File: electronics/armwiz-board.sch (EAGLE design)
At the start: 99 parts, among them J1 MICRO-SDCARD-CONNECTOR-330006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, J15 Cortex Debug, J16 ST-Link v2, J2 CORTEX_DEBUGSMD, U1 STM32F10XRXT6, U4 MIC5219-3.3V, X1 FH12-12S-1S, Y3 32.768kHz

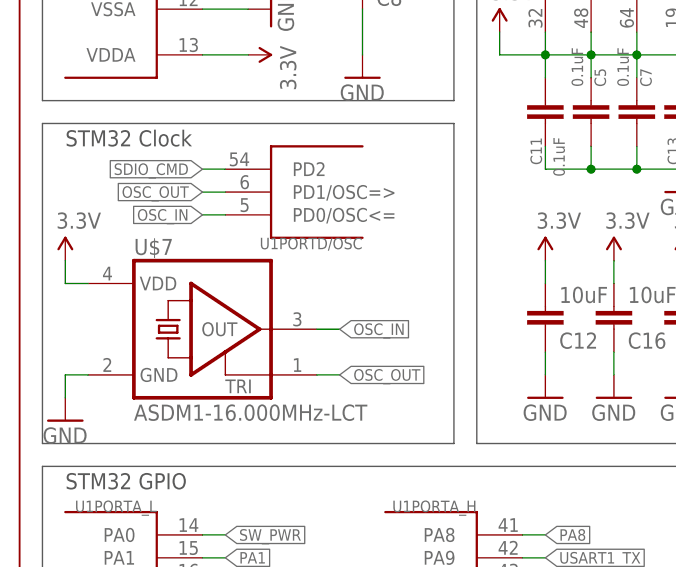
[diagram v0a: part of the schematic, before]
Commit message: Fixed MEMS oscillator issue. Closes #3.
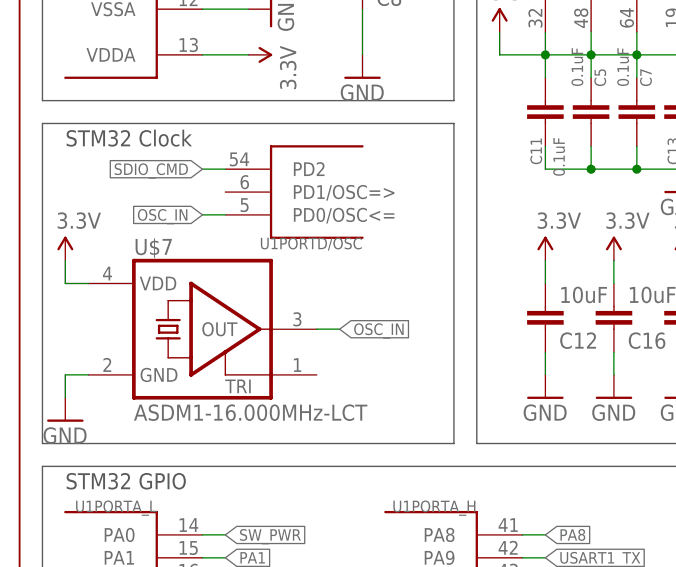
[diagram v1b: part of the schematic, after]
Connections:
- removed net OSC_OUT: U$7.TRI, U1PORTD/OSC.PD1/OSC=>
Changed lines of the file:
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@@
-</segment>
-</net>
-<net name="OSC_OUT" class="0">
-<segment>
-<pinref part="U1" gate="PORTD/OSC" pin="PD1/OSC=&gt;"/>
-<wire x1="30.48" y1="134.62" x2="27.94" y2="134.62" width="0.1524" layer="91"/>
-<label x="27.94" y="134.62" size="1.27" layer="95" rot="R180" xref="yes"/>
-</segment>
-<segment>
-<pinref part="U$7" gate="G$1" pin="TRI"/>
-<wire x1="40.64" y1="114.3" x2="43.18" y2="114.3" width="0.1524" layer="91"/>
-<label x="43.18" y="114.3" size="1.27" layer="95" xref="yes"/>
 </segment>
 </net>

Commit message: Board passes ERC and DRC.
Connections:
- removed net N$17: J2.GNDDTCT
- net GND: now also J2.GNDDTCT
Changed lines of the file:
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@@
 </variantdefs>
 <classes>
-<class number="0" name="default" width="0.075" drill="0.2">
+<class number="0" name="Digital signal" width="0.075" drill="0.2">
 <clearance class="0" value="0.075"/>
 </class>
-<class number="1" name="power" width="0.075" drill="0.2">
+<class number="1" name="3.3V power" width="0.075" drill="0.2">
 <clearance class="1" value="0.075"/>
+</class>
+<class number="2" name="RTC battery" width="0.075" drill="0.2">
+<clearance class="2" value="0.075"/>
+</class>
+<class number="3" name="5V power" width="0.075" drill="0.2">
+<clearance class="3" value="0.075"/>
+</class>
+<class number="4" name="Analog signal" width="0.075" drill="0.2">
+<clearance class="4" value="0.075"/>
+</class>
+<class number="5" name="Ground" width="0.075" drill="0.2">
+<clearance class="5" value="0.075"/>
 </class>
 </classes>
@@
 <wire x1="200.66" y1="152.4" x2="198.12" y2="152.4" width="0.1524" layer="91"/>
 <pinref part="J2" gate="G$1" pin="GND@3"/>
-<wire x1="198.12" y1="152.4" x2="198.12" y2="144.78" width="0.1524" layer="91"/>
+<wire x1="198.12" y1="152.4" x2="198.12" y2="147.32" width="0.1524" layer="91"/>
+<wire x1="198.12" y1="147.32" x2="198.12" y2="144.78" width="0.1524" layer="91"/>
 <wire x1="200.66" y1="154.94" x2="198.12" y2="154.94" width="0.1524" layer="91"/>
 <wire x1="198.12" y1="154.94" x2="198.12" y2="152.4" width="0.1524" layer="91"/>
 <junction x="198.12" y="152.4"/>
+<pinref part="J2" gate="G$1" pin="GNDDTCT"/>
+<wire x1="200.66" y1="147.32" x2="198.12" y2="147.32" width="0.1524" layer="91"/>
+<junction x="198.12" y="147.32"/>
 </segment>
 <segment>
@@
 </segment>
 </net>
-<net name="RTC_BAT" class="0">
+<net name="RTC_BAT" class="2">
 <segment>
 <pinref part="U1" gate="AN_POWER" pin="VBAT"/>
@@
 <pinref part="J2" gate="G$1" pin="SWDIO/TMS"/>
 <wire x1="238.76" y1="157.48" x2="233.68" y2="157.48" width="0.1524" layer="91"/>
-</segment>
-</net>
-<net name="N$17" class="0">
-<segment>
-<pinref part="J2" gate="G$1" pin="GNDDTCT"/>
-<wire x1="200.66" y1="147.32" x2="195.58" y2="147.32" width="0.1524" layer="91"/>
-<label x="195.58" y="147.32" size="1.27" layer="95" rot="R180" xref="yes"/>
 </segment>
 </net>
@@
 </sheet>
 </sheets>
+<errors>
+</errors>
 </schematic>
 </drawing>

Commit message: Changed to a metric layout. Moved to a 7x2 2.0mm module connector.
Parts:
- removed J$1: SMA_EDGE, SparkFun-Connectors:SMA_EDGE
- removed J10, J11, J12, J13, J19, J20, J21, J22, J23, J24, J26, J27, J3, J33, J4, J5, J6, J7, J8: (no value), SparkFun-Connectors:M01PTH
- removed J14: (no value), PaxInstruments-Connectors:M03X2PAX
- removed J15: Cortex Debug, SparkFun-Connectors:CORTEX_DEBUGSMD
- removed J16: ST-Link v2, SparkFun-Connectors:M10X2
- removed J17, J18: (no value), SparkFun-Connectors:M01NOSILK-KIT
- removed R23: 100R, resistor:R-US_R0402
- removed R24: 10K, resistor:R-US_R0402
- added C19, C20: 8pF, resistor:C-EUC0402K
- added C21: 10uF, resistor:C-EUC0402K
- added U$4, U$8, U$9: PAX_MODULE, PaxInstruments-Connectors:PAX_MODULE
- added Y1: 32.768kHz, SparkFun-FreqCtrl:CRYSTAL3.2X1.5MM
- U$7: value ASDM1-16.000MHz-LCT -> PAX_MODULE; device crystal:ASE -> PaxInstruments-Connectors:PAX_MODULE
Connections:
- net BOOT1 renamed (BOOT1)
- net MISO3 renamed PB4
- net MOSI3 renamed LCD_MOSI_(SPI3_MOSI)
- net RTC1 renamed RTC_OSC_IN
- net RTC2 renamed RTC_OSC_OUT
- net SCK3 renamed LCD_SCK_(SPI3_SCK)
- net SW_PWR renamed SW_PWR_(SYS_WKUP)
- net USB+ renamed USB_DP
- net USB- renamed USB_DM
- removed net AD_GND: J15.GND@3, J15.GND@5, J15.GNDDTCT, J16.10, J16.12, J16.14, J16.16, J16.18, J16.20, J16.4, J16.6, J16.8
- removed net AD_NRST: J15.NRESET, J16.15
- removed net AD_SWDCLK: J15.SWDCLK/TCK, J16.9
- removed net AD_SWDIO: J15.SWDIO/TMS, J16.7
- removed net AD_SWO: J15.SWO/TDO, J16.13
- removed net AD_TDI: J15.NC/TDI, J16.5
- removed net AD_VCC: J15.VCC, J16.1
- removed net LCD_A0: U1PORTB_H.PB9, X1-8.1
- removed net LCD_BL: R19.2, U1PORTB_L.PB6
- removed net LCD_CS: U1PORTB_L.PB7, X1-10.1
- removed net LCD_RST: U1PORTB_H.PB8, X1-9.1
- removed net MISO1: J10.1, U1PORTA_L.PA6
- removed net MOSI1: J13.1, U1PORTA_L.PA7
- removed net N$12: J2.SWO/TDO, R23.2
- removed net N$14: J$1.GND@1, J$1.GND@3, J26.1
- removed net N$15: J$1.GND@0, J$1.GND@2, J23.1
- removed net N$20: J$1.SIGNAL, J27.1
- removed net PA2: J3.1, U1PORTA_L.PA2
- removed net PA3: J12.1, U1PORTA_L.PA3
- removed net PA4: J5.1, U1PORTA_L.PA4
- removed net PB10: J24.1, U1PORTB_H.PB10
- removed net PC0: J20.1, U1PORTC_L.PC0
- removed net PC1: J22.1, U1PORTC_L.PC1
- removed net PC13: J21.1, U1PORTC_H.PC13
- removed net SCLK1: J4.1, U1PORTA_L.PA5
- removed net SWDCLK: J14.2, R18.1, R2.1, U1PORTA_H.PA14
- removed net SWO: J14.6, R23.1, R24.1, U1PORTA_H.PA15
- removed net VBAT2: R25.2, R26.1, U1PORTC_L.PC5
- new net 12C1_SDA: U1PORTB_L.PB7
- new net CAN_RX: U$4.CAN_RX, U$7.CAN_RX, U$8.CAN_RX, U$9.CAN_RX, U1PORTB_H.PB8
- new net CAN_TX: U$4.CAN_TX, U$7.CAN_TX, U$8.CAN_TX, U$9.CAN_TX, U1PORTB_H.PB9
- new net GPIO_(SPI1_NSS): U$8.GPIO0_(INT/A/D), U1PORTA_L.PA4
- new net GPIO_(SPI2_NSS): U$4.GPIO0_(INT/A/D), U1PORTB_H.PB12
- new net I2C1_SCL: U$4.I2C_SCL, U$7.I2C_SCL, U1PORTB_L.PB6
- new net I2C1_SDA: U$4.I2C_SDA, U$7.I2C_SDA
- new net I2C2_SCL: U$8.I2C_SCL, U$9.I2C_SCL, U1PORTB_H.PB10
- new net I2C2_SDA: U$8.I2C_SDA, U$9.I2C_SDA, U1PORTB_H.PB11
- new net LCD_A0_(GPIO): U1PORTC_L.PC1, X1-8.1
- new net LCD_BL_(GPIO): R19.2, U1PORTC_L.PC0
- new net LCD_CS_(SPI3_NSS): U1PORTA_H.PA15, X1-10.1
- new net LCD_RST_(GPIO): U1PORTC_H.PC13, X1-9.1
- new net LED2: LED2.A
- new net N$51: U$8.GPIO1_(INT/A/D)
- new net N$52: U$8.GPIO2_(INT/A/D)
- new net N$57: U$4.GPIO1_(INT/A/D)
- new net N$58: U$4.GPIO2_(INT/A/D)
- new net N$68: U$7.GPIO0_(INT/A/D)
- new net N$69: U$7.GPIO1_(INT/A/D)
- new net N$70: U$7.GPIO2_(INT/A/D)
- new net N$74: U$9.GPIO0_(INT/A/D)
- new net N$75: U$9.GPIO1_(INT/A/D)
- new net N$76: U$9.GPIO2_(INT/A/D)
- new net OSC_OUT: C19.1, U1PORTD/OSC.PD1/OSC=>, Y1.1
- new net PC5: U1PORTC_L.PC5
- new net PC6: U1PORTC_L.PC6
- new net PC7: U1PORTC_L.PC7
- new net SPI1_MISO: U$8.SPI_MISO, U$9.SPI_MISO, U1PORTA_L.PA6
- new net SPI1_MOSI: U$8.SPI_MOSI, U$9.SPI_MOSI, U1PORTA_L.PA7
- new net SPI1_SCK: U$8.SPI_SCK, U$9.SPI_SCK, U1PORTA_L.PA5
- new net SPI2_MISO: U$4.SPI_MISO, U$7.SPI_MISO, U1PORTB_H.PB14
- new net SPI2_MOSI: U$4.SPI_MOSI, U$7.SPI_MOSI, U1PORTB_H.PB15
- new net SPI2_SCK: U$4.SPI_SCK, U$7.SPI_SCK, U1PORTB_H.PB13
- new net SWCLK: R18.1, R2.1, U1PORTA_H.PA14
- new net USART2_RX: U$4.USART_RX, U$7.USART_RX, U$8.USART_RX, U$9.USART_RX, U1PORTA_L.PA3
- new net USART2_TX: U$4.USART_TX, U$7.USART_TX, U$8.USART_TX, U$9.USART_TX, U1PORTA_L.PA2
- new net VBAT_1/2: R25.2, R26.1
- net 3.3V: now also C21.2, U$4.3V3, U$7.3V3, U$8.3V3, U$9.3V3; no longer J14.1, J18.1, R24.2, U$7.VDD
- net BOOT0: no longer J17.1
- net GND: now also C19.2, C20.2, C21.1, U$4.GND, U$8.GND, U$9.GND; no longer J14.3
- net NRST: no longer J14.5
- net OSC_IN: now also C20.1, Y1.2; no longer U$7.OUT
- net PA1: no longer J19.1
- net PA8: no longer LED2.A
- net PB0: no longer J6.1
- net PB1: no longer J11.1
- net PC2: no longer J33.1
- net PC3: no longer J7.1
- net PC4: no longer J8.1
- net SD_DETECT: no longer U1PORTB_H.PB14
- net SWDIO: no longer J14.4
- net SW_A: no longer U1PORTB_H.PB15
- net SW_B: no longer U1PORTC_L.PC6
- net SW_C: no longer U1PORTC_L.PC7
- net SW_D: no longer U1PORTB_H.PB12
- net SW_E: no longer U1PORTB_H.PB13
- net VBUS: no longer U1PORTB_H.PB11
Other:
- note added: "Breakout Headers"
- note added: "Orphin Nets"
- note removed: "Board edgs SMA connector"
- note removed: "Breakout Header"
- note removed: "Cortex Debug Adapter"
- note removed: "Testing Suff"
- moved on the sheet: BAT1, C14, C6, C9, J1, R13, R14, R17, R5, R6, R7, Y3

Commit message: Updated board with new Pax Instruments library parts.
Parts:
- removed U$4, U$7, U$8, U$9: PAX_MODULE, PaxInstruments-Connectors:PAX_MODULE
- removed X1: FH12-12S-1S, PaxInstrument-T400:FH12-12S-1S
- added MODULE1, MODULE2, MODULE3, MODULE4: PI-module-female, PaxInstruments-Connectors:PAX_MODULE_EDGE_FEMALE_HOST
- added X2: M12_BOTTOM_CONTACTS_FPC_1MM, PaxInstruments-Connectors:M12_BOTTOM_CONTACTS_FPC_1MM
- C1: device resistor:C-EUC0402K -> PaxInstruments-Capacitors:C0402_4.7UF
- C10, C11, C13, C14, C15, C18, C2, C27, C3, C5, C7, C8: device resistor:C-EUC0402K -> PaxInstruments-Capacitors:C0402_100NF
- C12, C16, C17, C21, C26: device resistor:C-EUC0402K -> PaxInstruments-Capacitors:C0402_10UF
- C19, C20, C6, C9: device resistor:C-EUC0402K -> PaxInstruments-Capacitors:C0402_8PF
- C35, C36: device resistor:C-EUC0402K -> PaxInstruments-Capacitors:C0402_1UF
- C4: device resistor:C-EUC0402K -> PaxInstruments-Capacitors:C0402_470PF
- J1: value MICRO-SDCARD-CONNECTOR-3300060P1 -> MICROSD; device PaxInstrument-T400:MICRO-SDCARD-CONNECTOR-3300060P1 -> PaxInstruments-Connectors:MICROSD; MF SUNTECH -> (none)
- R1, R11, R12, R15, R16, R8: value 10k -> 10K; device resistor:R-US_R0402 -> PaxInstruments-Resistors:R0402_10K; POPULATE DNP -> (none)
- R10, R9: device resistor:R-US_R0402 -> PaxInstruments-Resistors:R0402_22R
- R13, R14, R17, R2, R21, R25, R26, R4, R5, R6, R7: device resistor:R-US_R0402 -> PaxInstruments-Resistors:R0402_10K
- R18, R20: device resistor:R-US_R0402 -> PaxInstruments-Resistors:R0402_100R
- R19: device resistor:R-US_R0402 -> PaxInstruments-Resistors:R0402_3.3R
- R22, R3: device resistor:R-US_R0402 -> PaxInstruments-Resistors:R0402_360R
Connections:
- removed net 12C1_SDA: U1PORTB_L.PB7
- removed net N$52: U$8.GPIO2_(INT/A/D)
- removed net N$58: U$4.GPIO2_(INT/A/D)
- removed net N$70: U$7.GPIO2_(INT/A/D)
- removed net N$76: U$9.GPIO2_(INT/A/D)
- removed net PB4: U1PORTB_L.PB4
- new net PC0: U1PORTC_L.PC0
- net 3.3V: now also C11.1, C12.1, C13.1, C16.1, C17.1, C21.1, C26.2, C27.2, C8.1, MODULE1.3V3, MODULE2.3V3, MODULE3.3V3, MODULE4.3V3, R13.2, R14.2, R17.2, R5.2, R6.2, R7.2, X2.12, X2.5; no longer C11.2, C12.2, C13.2, C16.2, C17.2, C21.2, C26.1, C27.1, C8.2, R13.1, R14.1, R17.1, R5.1, R6.1, R7.1, U$4.3V3, U$7.3V3, U$8.3V3, U$9.3V3, X1-12.1, X1-5.1
- net CAN_RX: now also MODULE1.CAN_RX, MODULE2.CAN_RX, MODULE3.CAN_RX, MODULE4.CAN_RX; no longer U$4.CAN_RX, U$7.CAN_RX, U$8.CAN_RX, U$9.CAN_RX
- net CAN_TX: now also MODULE1.CAN_TX, MODULE2.CAN_TX, MODULE3.CAN_TX, MODULE4.CAN_TX; no longer U$4.CAN_TX, U$7.CAN_TX, U$8.CAN_TX, U$9.CAN_TX
- net GND: now also C1.1, C11.2, C12.2, C13.2, C16.2, C17.2, C2.1, C21.2, C26.1, C27.1, C8.2, J1.GND1, J1.GND2, J1.GND3, J1.GND4, MODULE1.GND, MODULE1.KEY, MODULE2.GND, MODULE2.KEY, MODULE3.GND, MODULE3.KEY, MODULE4.GND, MODULE4.KEY, R1.1, R22.2, R3.2, X2.4; no longer C1.2, C11.1, C12.1, C13.1, C16.1, C17.1, C2.2, C21.1, C26.2, C27.2, C8.1, J1.G1, J1.G2, J1.G3, J1.G4, R1.2, R22.1, R3.1, U$4.GND, U$7.GND, U$8.GND, U$9.GND, X1-4.1
- net GPIO_(SPI1_NSS): now also MODULE3.GPIO0; no longer U$8.GPIO0_(INT/A/D)
- net GPIO_(SPI2_NSS): now also MODULE1.GPIO0; no longer U$4.GPIO0_(INT/A/D)
- net I2C1_SCL: now also MODULE1.I2C_SCL, MODULE2.I2C_SCL; no longer U$4.I2C_SCL, U$7.I2C_SCL
- net I2C1_SDA: now also MODULE1.I2C_SDA, MODULE2.I2C_SDA, U1PORTB_L.PB7; no longer U$4.I2C_SDA, U$7.I2C_SDA
- net I2C2_SCL: now also MODULE3.I2C_SCL, MODULE4.I2C_SCL; no longer U$8.I2C_SCL, U$9.I2C_SCL
- net I2C2_SDA: now also MODULE3.I2C_SDA, MODULE4.I2C_SDA; no longer U$8.I2C_SDA, U$9.I2C_SDA
- net LCD_A0_(GPIO): now also X2.8; no longer X1-8.1
- net LCD_BL_(GPIO): now also U1PORTB_L.PB4; no longer U1PORTC_L.PC0
- net LCD_CS_(SPI3_NSS): now also X2.10; no longer X1-10.1
- net LCD_MOSI_(SPI3_MOSI): now also X2.6; no longer X1-6.1
- net LCD_RST_(GPIO): now also X2.9; no longer X1-9.1
- net LCD_SCK_(SPI3_SCK): now also X2.7; no longer X1-7.1
- net N$11: now also R22.1; no longer R22.2
- net N$37: now also X2.3; no longer X1-3.1
- net N$38: now also X2.2; no longer X1-2.1
- net N$39: now also X2.1; no longer X1-1.1
- net N$4: now also X2.11; no longer X1-11.1
- net N$51: now also MODULE3.GPIO1; no longer U$8.GPIO1_(INT/A/D)
- net N$57: now also MODULE1.GPIO1; no longer U$4.GPIO1_(INT/A/D)
- net N$68: now also MODULE2.GPIO0; no longer U$7.GPIO0_(INT/A/D)
- net N$69: now also MODULE2.GPIO1; no longer U$7.GPIO1_(INT/A/D)
- net N$7: now also R3.1; no longer R3.2
- net N$74: now also MODULE4.GPIO0; no longer U$9.GPIO0_(INT/A/D)
- net N$75: now also MODULE4.GPIO1; no longer U$9.GPIO1_(INT/A/D)
- net SDIO_CLK: now also J1.SDIO_CLK, R7.1; no longer J1.SCLK, R7.2
- net SDIO_CMD: now also J1.SDIO_CMD, R14.1; no longer J1.DI, R14.2
- net SDIO_D0: now also J1.SDIO_D0, R13.1; no longer J1.DO, R13.2
- net SDIO_D1: now also J1.SDIO_D1, R17.1; no longer J1.DATA1, R17.2
- net SDIO_D2: now also J1.SDIO_D2, R5.1; no longer J1.DATA2, R5.2
- net SDIO_D3: now also J1.SDIO_D3, R6.1; no longer J1.CS, R6.2
- net SD_DETECT: now also J1.DETECT; no longer J1.CDN
- net SPI1_MISO: now also MODULE3.SPI_MISO, MODULE4.SPI_MISO; no longer U$8.SPI_MISO, U$9.SPI_MISO
- net SPI1_MOSI: now also MODULE3.SPI_MOSI, MODULE4.SPI_MOSI; no longer U$8.SPI_MOSI, U$9.SPI_MOSI
- net SPI1_SCK: now also MODULE3.SPI_SCK, MODULE4.SPI_SCK; no longer U$8.SPI_SCK, U$9.SPI_SCK
- net SPI2_MISO: now also MODULE1.SPI_MISO, MODULE2.SPI_MISO; no longer U$4.SPI_MISO, U$7.SPI_MISO
- net SPI2_MOSI: now also MODULE1.SPI_MOSI, MODULE2.SPI_MOSI; no longer U$4.SPI_MOSI, U$7.SPI_MOSI
- net SPI2_SCK: now also MODULE1.SPI_SCK, MODULE2.SPI_SCK; no longer U$4.SPI_SCK, U$7.SPI_SCK
- net SW_PWR_(SYS_WKUP): now also R1.2; no longer R1.1
- net USART2_RX: now also MODULE1.UART_RX, MODULE2.UART_RX, MODULE3.UART_RX, MODULE4.UART_RX; no longer U$4.USART_RX, U$7.USART_RX, U$8.USART_RX, U$9.USART_RX
- net USART2_TX: now also MODULE1.UART_TX, MODULE2.UART_TX, MODULE3.UART_TX, MODULE4.UART_TX; no longer U$4.USART_TX, U$7.USART_TX, U$8.USART_TX, U$9.USART_TX
- net VBUS: now also C1.2, C2.2; no longer C1.1, C2.1
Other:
- note added: "Module Connectors"
- note removed: "Breakout Headers"
- moved on the sheet: BAT1, C1, C10, C11, C12, C13, C14, C15, C16, C17, C18, C19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

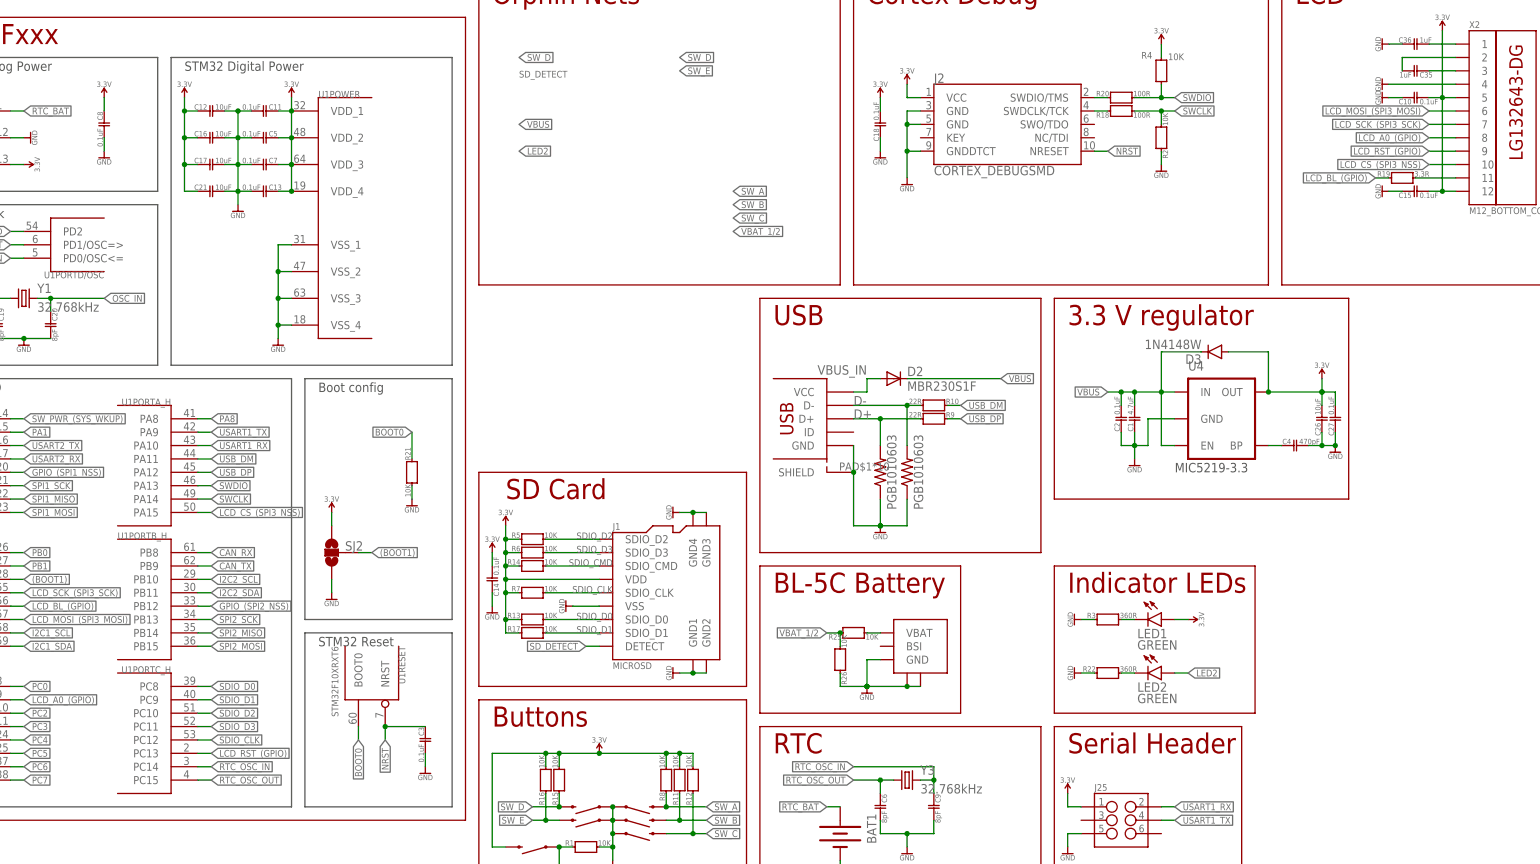
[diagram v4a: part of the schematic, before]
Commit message: Signals routed to the module headers.
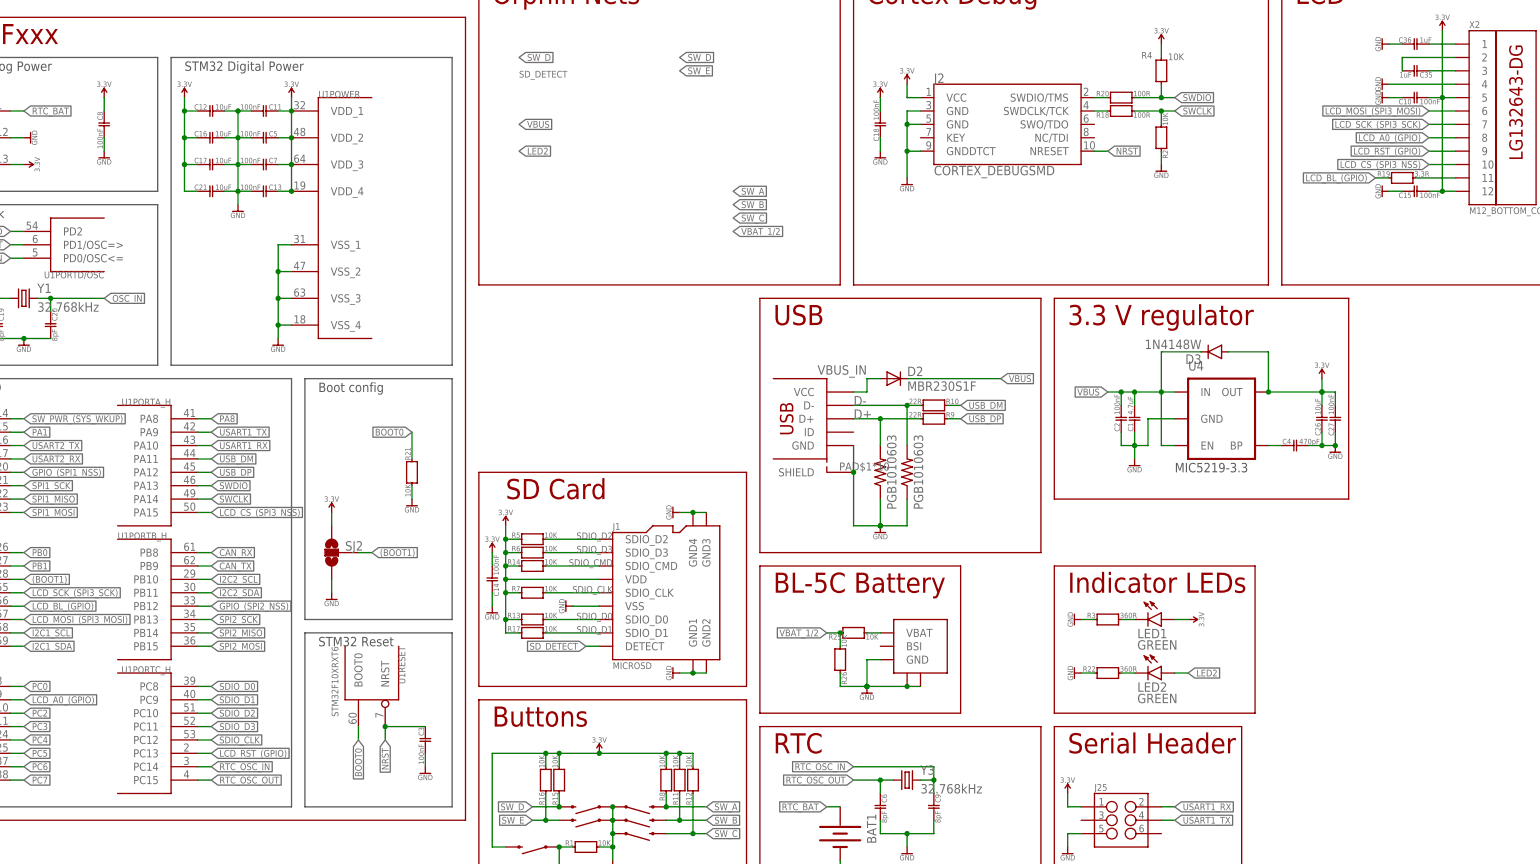
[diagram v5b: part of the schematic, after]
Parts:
- C1: device PaxInstruments-Capacitors:C0402_4.7UF -> PaxInstruments-RCL:C0402_4.7UF
- C10, C11, C13, C14, C15, C18, C2, C27, C3, C5, C7, C8: value 0.1uF -> 100nF; device PaxInstruments-Capacitors:C0402_100NF -> PaxInstruments-RCL:C0402_100NF
- C12, C16, C17, C21, C26: device PaxInstruments-Capacitors:C0402_10UF -> PaxInstruments-RCL:C0402_10UF
- C19, C20, C6, C9: device PaxInstruments-Capacitors:C0402_8PF -> PaxInstruments-RCL:C0402_8PF
- C35, C36: device PaxInstruments-Capacitors:C0402_1UF -> PaxInstruments-RCL:C0402_1UF
- C4: device PaxInstruments-Capacitors:C0402_470PF -> PaxInstruments-RCL:C0402_470PF
- R1, R11, R12, R13, R14, R15, R16, R17, R2, R21, R25, R26, R4, R5, R6, R7, R8: device PaxInstruments-Resistors:R0402_10K -> PaxInstruments-RCL:R0402_10K
- R18, R20: device PaxInstruments-Resistors:R0402_100R -> PaxInstruments-RCL:R0402_100R
- R19: device PaxInstruments-Resistors:R0402_3.3R -> PaxInstruments-RCL:R0402_3.3R
- R22, R3: device PaxInstruments-Resistors:R0402_360R -> PaxInstruments-RCL:R0402_360R
